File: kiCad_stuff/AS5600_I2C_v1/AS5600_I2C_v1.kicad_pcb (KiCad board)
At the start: 2 copper layers, 8 parts, among them J1 Conn_01x04, U1 AS5600_ASOM_v1

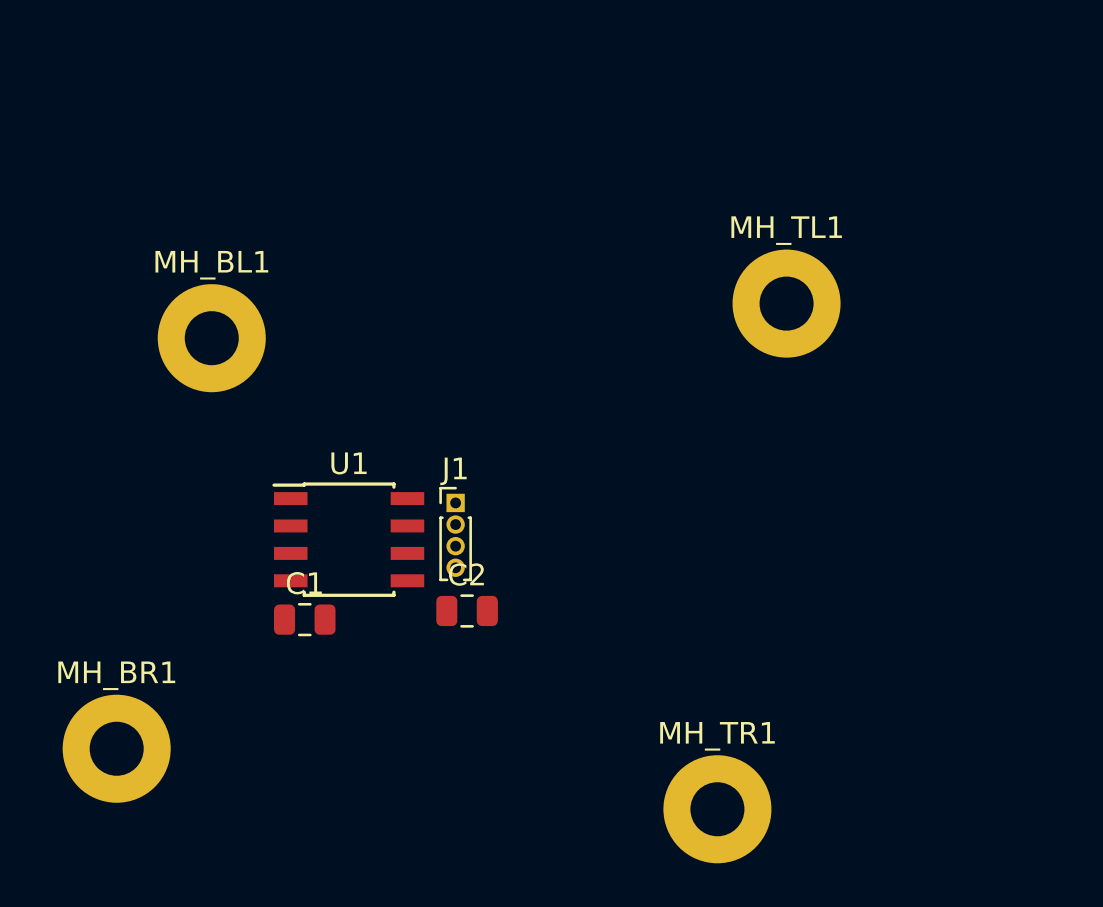
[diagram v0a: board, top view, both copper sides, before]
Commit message: Added proj footptint symbol lib with 2 user-made footprints
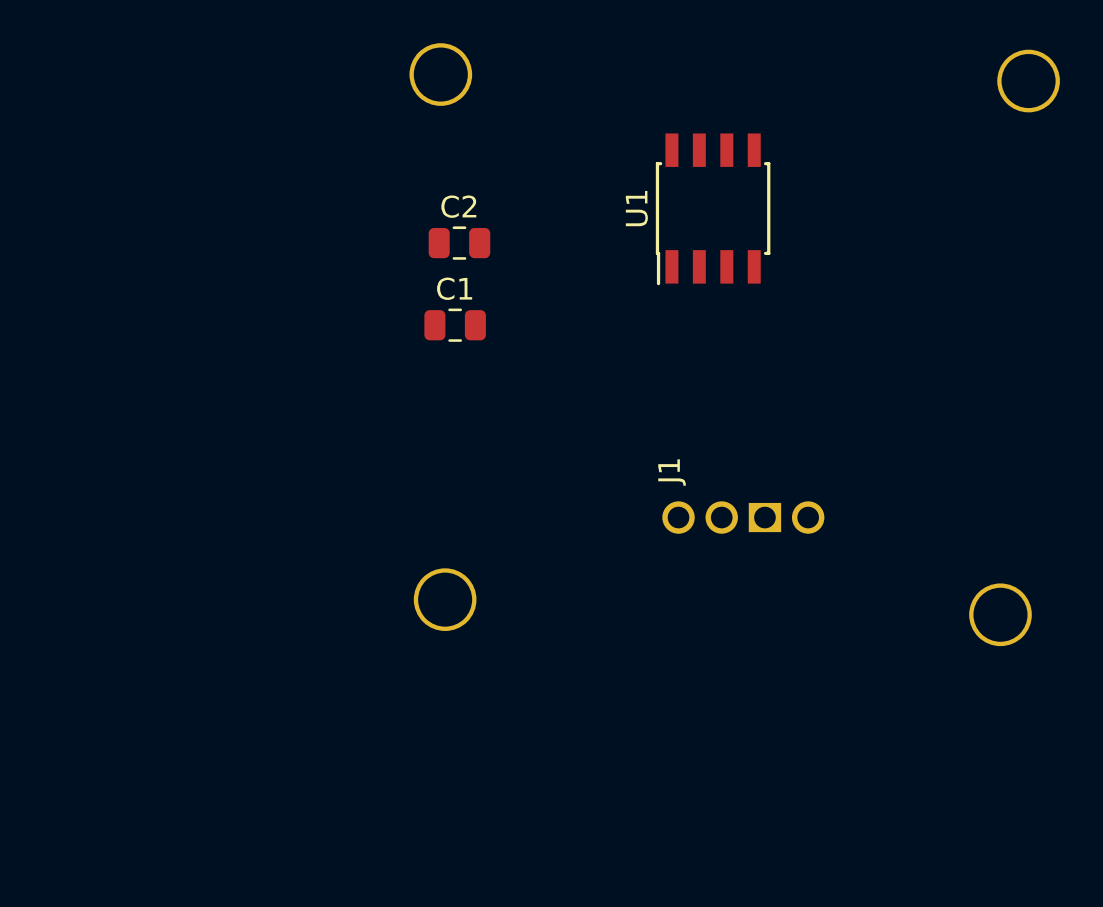
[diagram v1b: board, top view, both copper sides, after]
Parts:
- removed MH_BL1, MH_BR1, MH_TL1, MH_TR1: MountingHole, MountingHole:MountingHole_2.5mm_Pad
- added 2.5mm : Hole_TR, modular_segment_PCB_footprints:MountingHole_2.5mm_Pad, F.Cu at (184.2, 63.1)
- added 2.5mm : Hole_TL, modular_segment_PCB_footprints:MountingHole_2.5mm_Pad, F.Cu at (157.0, 62.8)
- added 2.5mm : Hole_BL, modular_segment_PCB_footprints:MountingHole_2.5mm_Pad, F.Cu at (157.2, 87.1)
- added 2.5mm : Hole_BR, modular_segment_PCB_footprints:MountingHole_2.5mm_Pad, F.Cu at (182.9, 87.8)
- J1: footprint Connector_PinHeader_1.00mm:PinHeader_1x04_P1.00mm_Vertical -> modular_segment_PCB_footprints:EthernetWireConnectors_1x04_P2.00mm_1mmDiam
- moved U1 22.8 mm to (169.6, 69.0), turned to 90 degrees
- moved C2 17.0 mm to (157.9, 70.6)
- moved C1 15.3 mm to (157.7, 74.4)
- moved J1 12.3 mm to (170.0, 83.3), turned to 90 degrees
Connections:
- U1 pad 5: (no net) -> Net-(U1-Pad5)

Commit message: Parts except pins in position
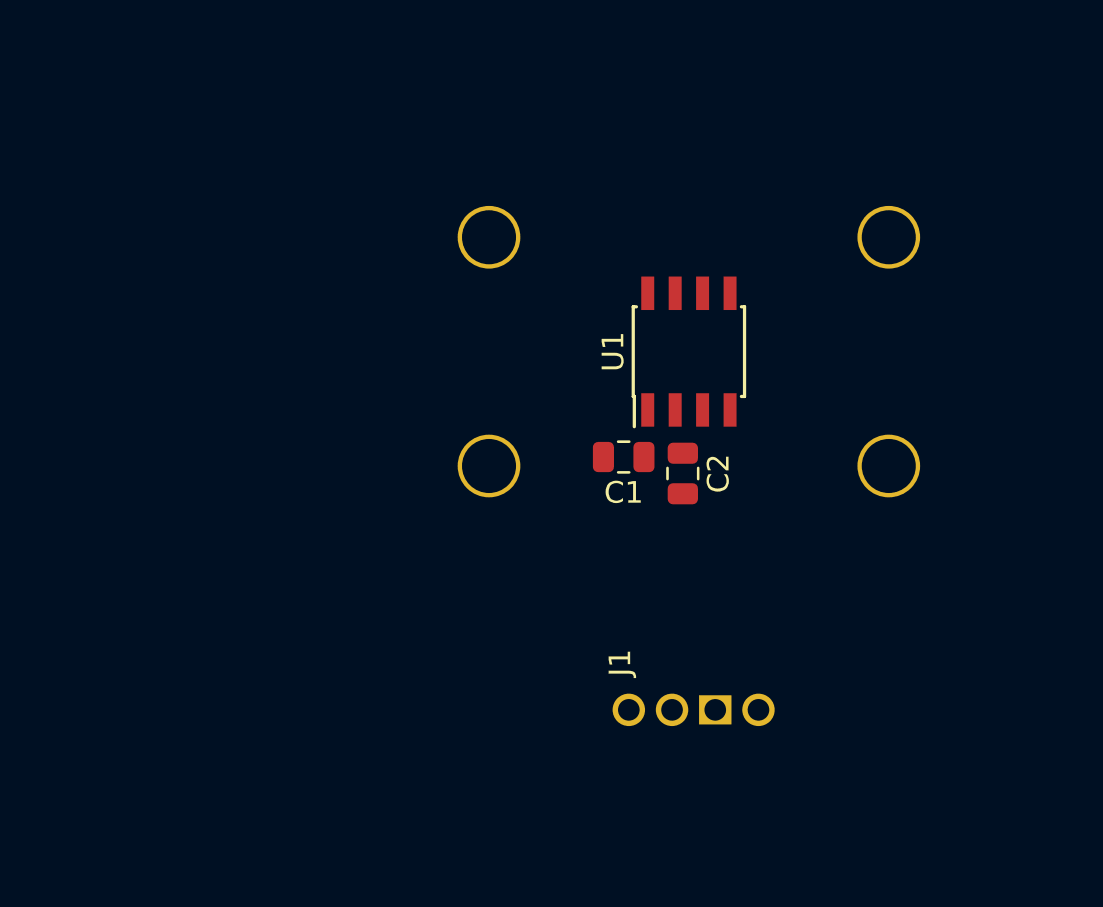
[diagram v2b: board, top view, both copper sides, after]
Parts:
- removed the 2.5mm  at (157.0, 62.8)
- removed the 2.5mm  at (157.2, 87.1)
- added 2.5mm : Hole_TL, modular_segment_PCB_footprints:MountingHole_2.5mm_Pad, F.Cu at (159.2, 70.3)
- added 2.5mm : Hole_BL, modular_segment_PCB_footprints:MountingHole_2.5mm_Pad, F.Cu at (159.2, 80.9)
- moved C2 14.9 mm to (168.2, 81.3), turned to 270 degrees
- moved C1 9.90 mm to (165.5, 80.5), turned to 180 degrees
- moved 2.5mm  9.70 mm to (177.7, 70.3)
- moved J1 9.19 mm to (167.7, 92.2)
- moved 2.5mm  8.61 mm to (177.7, 80.9)
- moved U1 6.72 mm to (168.5, 75.6)
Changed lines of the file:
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@@
     (pad_to_mask_clearance 0.2)
     (aux_axis_origin 0 0)
+    (grid_origin 152 59)
     (visible_elements 7FFFFFFF)
     (pcbplotparams
@@
     (add_net SDA)
   )
-  (module Capacitor_SMD:C_0805_2012Metric (layer F.Cu)
-    (at 157.6625 74.4)
+  (module Capacitor_SMD:C_0805_2012Metric locked (layer F.Cu)
+    (at 165.4625 80.5 180)
     (descr "Capacitor SMD 0805 (2012 Metric), square (rectangular) end terminal, IPC_7351 nominal, (Body size source: https://docs.google.com/spreadsheets/d/1BsfQQcO9C6DZCsRaXUlFlo91Tg2WpOkGARC1WS5S8t0/edit?usp=sharing), generated with kicad-footprint-generator")
     (tags capacitor)
     (attr smd)
-    (fp_text reference C1 (at 0 -1.65) (layer F.SilkS)
-      (effects (font (size 1 1) (thickness 0.15)))
-    )
-    (fp_text value 100nF (at 0 1.65) (layer F.Fab)
+    (fp_text reference C1 (at 0 -1.65 180) (layer F.SilkS)
+      (effects (font (size 1 1) (thickness 0.15)))
+    )
+    (fp_text value 100nF (at 0 1.65 180) (layer F.Fab)
       (effects (font (size 1 1) (thickness 0.15)))
     )
@@
     (fp_line (start 1.68 -0.95) (end 1.68 0.95) (layer F.CrtYd) (width 0.05))
     (fp_line (start 1.68 0.95) (end -1.68 0.95) (layer F.CrtYd) (width 0.05))
-    (fp_text user %R (at 0 0) (layer F.Fab)
+    (fp_text user %R (at 0 0 180) (layer F.Fab)
       (effects (font (size 0.5 0.5) (thickness 0.08)))
     )
-    (pad 1 smd roundrect (at -0.9375 0) (size 0.975 1.4) (layers F.Cu F.Paste F.Mask) (roundrect_rratio 0.25)
+    (pad 1 smd roundrect (at -0.9375 0 180) (size 0.975 1.4) (layers F.Cu F.Paste F.Mask) (roundrect_rratio 0.25)
       (net 1 +5V))
-    (pad 2 smd roundrect (at 0.9375 0) (size 0.975 1.4) (layers F.Cu F.Paste F.Mask) (roundrect_rratio 0.25)
+    (pad 2 smd roundrect (at 0.9375 0 180) (size 0.975 1.4) (layers F.Cu F.Paste F.Mask) (roundrect_rratio 0.25)
       (net 2 GND))
     (model ${KISYS3DMOD}/Capacitor_SMD.3dshapes/C_0805_2012Metric.wrl
@@
     )
   )
-  (module Capacitor_SMD:C_0805_2012Metric (layer F.Cu)
-    (at 157.8625 70.6)
+  (module Capacitor_SMD:C_0805_2012Metric locked (layer F.Cu)
+    (at 168.2 81.2625 270)
     (descr "Capacitor SMD 0805 (2012 Metric), square (rectangular) end terminal, IPC_7351 nominal, (Body size source: https://docs.google.com/spreadsheets/d/1BsfQQcO9C6DZCsRaXUlFlo91Tg2WpOkGARC1WS5S8t0/edit?usp=sharing), generated with kicad-footprint-generator")
     (tags capacitor)
     (attr smd)
-    (fp_text reference C2 (at 0 -1.65) (layer F.SilkS)
-      (effects (font (size 1 1) (thickness 0.15)))
-    )
-    (fp_text value 1uF (at 0 1.65) (layer F.Fab)
-      (effects (font (size 1 1) (thickness 0.15)))
-    )
-    (fp_text user %R (at 0 0) (layer F.Fab)
+    (fp_text reference C2 (at 0 -1.65 270) (layer F.SilkS)
+      (effects (font (size 1 1) (thickness 0.15)))
+    )
+    (fp_text value 1uF (at 0 1.65 270) (layer F.Fab)
+      (effects (font (size 1 1) (thickness 0.15)))
+    )
+    (fp_text user %R (at 0 0 270) (layer F.Fab)
       (effects (font (size 0.5 0.5) (thickness 0.08)))
     )
@@
     (fp_line (start -1 -0.6) (end 1 -0.6) (layer F.Fab) (width 0.1))
     (fp_line (start -1 0.6) (end -1 -0.6) (layer F.Fab) (width 0.1))
-    (pad 2 smd roundrect (at 0.9375 0) (size 0.975 1.4) (layers F.Cu F.Paste F.Mask) (roundrect_rratio 0.25)
-      (net 2 GND))
-    (pad 1 smd roundrect (at -0.9375 0) (size 0.975 1.4) (layers F.Cu F.Paste F.Mask) (roundrect_rratio 0.25)
+    (pad 2 smd roundrect (at 0.9375 0 270) (size 0.975 1.4) (layers F.Cu F.Paste F.Mask) (roundrect_rratio 0.25)
+      (net 2 GND))
+    (pad 1 smd roundrect (at -0.9375 0 270) (size 0.975 1.4) (layers F.Cu F.Paste F.Mask) (roundrect_rratio 0.25)
       (net 3 "Net-(C2-Pad1)"))
     (model ${KISYS3DMOD}/Capacitor_SMD.3dshapes/C_0805_2012Metric.wrl
@@
   )
   (module modular_segment_PCB_footprints:EthernetWireConnectors_1x04_P2.00mm_1mmDiam (layer F.Cu)
-    (at 170 83.3 90)
+    (at 167.7 92.2 90)
     (descr "Through hole straight pin header, 1x04, 1.00mm pitch, single row")
     (tags "Through hole pin header THT 1x04 1.00mm single row")
@@
     )
   )
-  (module Package_SO:SOIC-8_3.9x4.9mm_P1.27mm (layer F.Cu)
-    (at 169.6 69 90)
+  (module Package_SO:SOIC-8_3.9x4.9mm_P1.27mm locked (layer F.Cu)
+    (at 168.48 75.622 90)
     (descr "8-Lead Plastic Small Outline (SN) - Narrow, 3.90 mm Body [SOIC] (see Microchip Packaging Specification 00000049BS.pdf)")
     (tags "SOIC 1.27")
@@
     )
   )
-  (module modular_segment_PCB_footprints:MountingHole_2.5mm_Pad (layer F.Cu)
-    (at 184.2 63.1)
+  (module modular_segment_PCB_footprints:MountingHole_2.5mm_Pad locked (layer F.Cu)
+    (at 177.73 70.33)
     (descr "Mounting Hole 2.5mm")
     (tags "mounting hole 2.5mm")
@@
     (pad "" np_thru_hole circle (at 0 0) (size 2.9 2.9) (drill 2.5) (layers *.Cu *.Mask))
   )
-  (module modular_segment_PCB_footprints:MountingHole_2.5mm_Pad (layer F.Cu)
-    (at 157 62.8)
+  (module modular_segment_PCB_footprints:MountingHole_2.5mm_Pad locked (layer F.Cu)
+    (at 159.23 70.33)
     (descr "Mounting Hole 2.5mm")
     (tags "mounting hole 2.5mm")
@@
     (pad "" np_thru_hole circle (at 0 0) (size 2.9 2.9) (drill 2.5) (layers *.Cu *.Mask))
   )
-  (module modular_segment_PCB_footprints:MountingHole_2.5mm_Pad (layer F.Cu)
-    (at 157.2 87.1)
+  (module modular_segment_PCB_footprints:MountingHole_2.5mm_Pad locked (layer F.Cu)
+    (at 159.23 80.915)
     (descr "Mounting Hole 2.5mm")
     (tags "mounting hole 2.5mm")
@@
     (pad "" np_thru_hole circle (at 0 0) (size 2.9 2.9) (drill 2.5) (layers *.Cu *.Mask))
   )
-  (module modular_segment_PCB_footprints:MountingHole_2.5mm_Pad (layer F.Cu)
-    (at 182.9 87.8)
-    (descr "Mounting Hole 2.5mm")
-    (tags "mounting hole 2.5mm")
+  (module modular_segment_PCB_footprints:MountingHole_2.5mm_Pad locked (layer F.Cu)
+    (at 177.73 80.915)
+    (descr "Mounting Hole 2.5mm")
+    (tags "mounting hole 2.5mm")

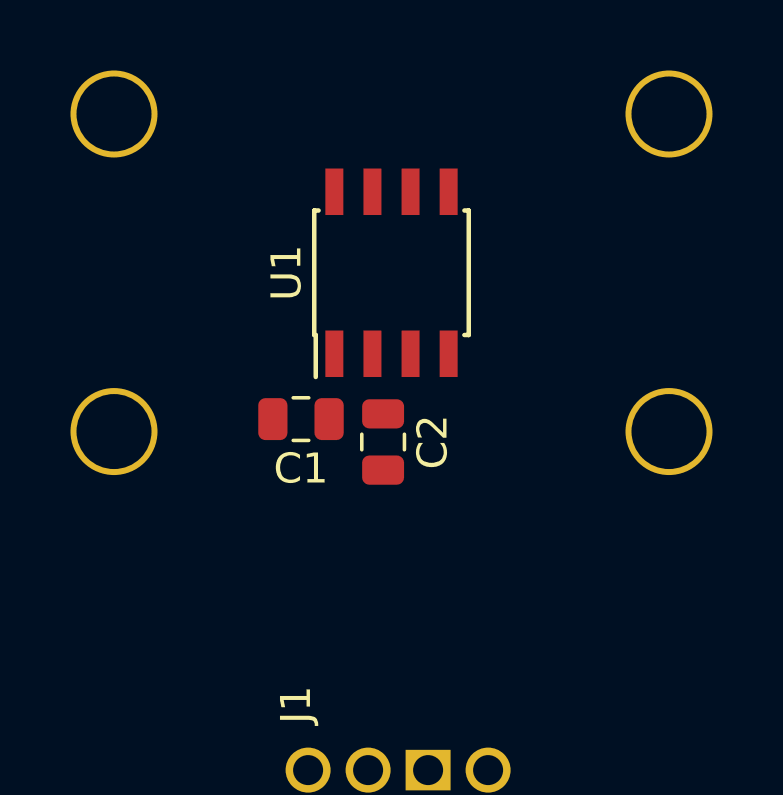
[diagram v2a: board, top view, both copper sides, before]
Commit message: Added PCB perimeter
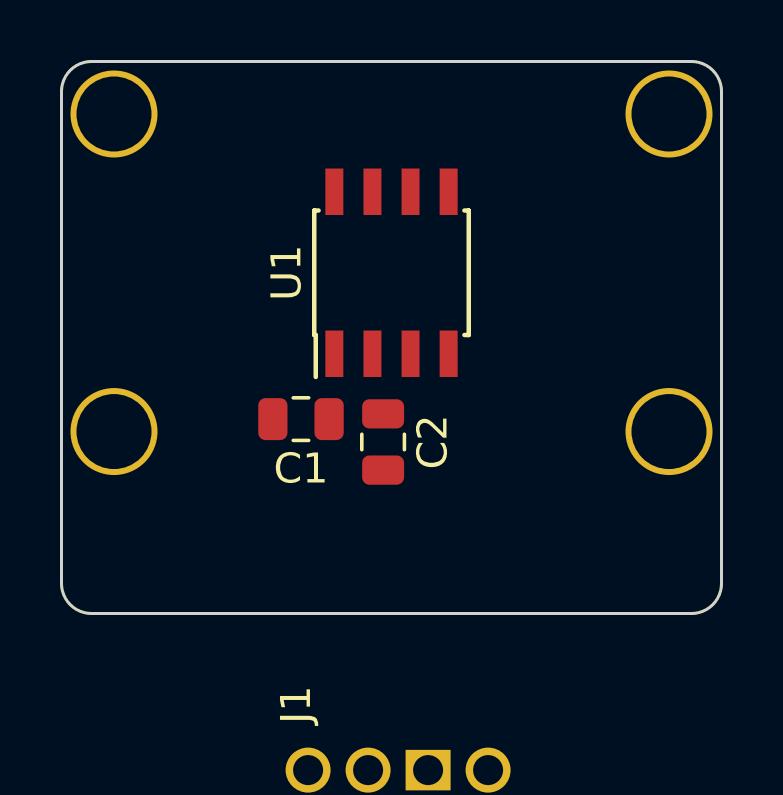
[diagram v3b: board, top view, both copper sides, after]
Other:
- board outline added: 22 x 18.4 mm
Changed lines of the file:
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@@
   (general
     (thickness 1.6)
-    (drawings 0)
+    (drawings 8)
     (tracks 0)
     (zones 0)
@@
     (trace_min 0.2)
     (segment_width 0.2)
-    (edge_width 0.15)
+    (edge_width 0.1)
     (via_size 0.8)
     (via_drill 0.4)
@@
     (pad "" np_thru_hole circle (at 0 0) (size 2.9 2.9) (drill 2.5) (layers *.Cu *.Mask))
   )
+  (gr_arc (start 178.48 69.58) (end 179.48 69.58) (angle -90) (layer Edge.Cuts) (width 0.1))
+  (gr_arc (start 158.48 69.58) (end 158.48 68.58) (angle -90) (layer Edge.Cuts) (width 0.1))
+  (gr_arc (start 158.48 85.98) (end 157.48 85.98) (angle -90) (layer Edge.Cuts) (width 0.1))
+  (gr_arc (start 178.48 85.98) (end 178.48 86.98) (angle -90) (layer Edge.Cuts) (width 0.1))
+  (gr_line (start 157.48 69.58) (end 157.48 85.98) (layer Edge.Cuts) (width 0.1))
+  (gr_line (start 158.48 86.98) (end 178.48 86.98) (layer Edge.Cuts) (width 0.1))
+  (gr_line (start 179.48 85.98) (end 179.48 69.58) (layer Edge.Cuts) (width 0.1))
+  (gr_line (start 178.48 68.58) (end 158.48 68.58) (layer Edge.Cuts) (width 0.1))
 )

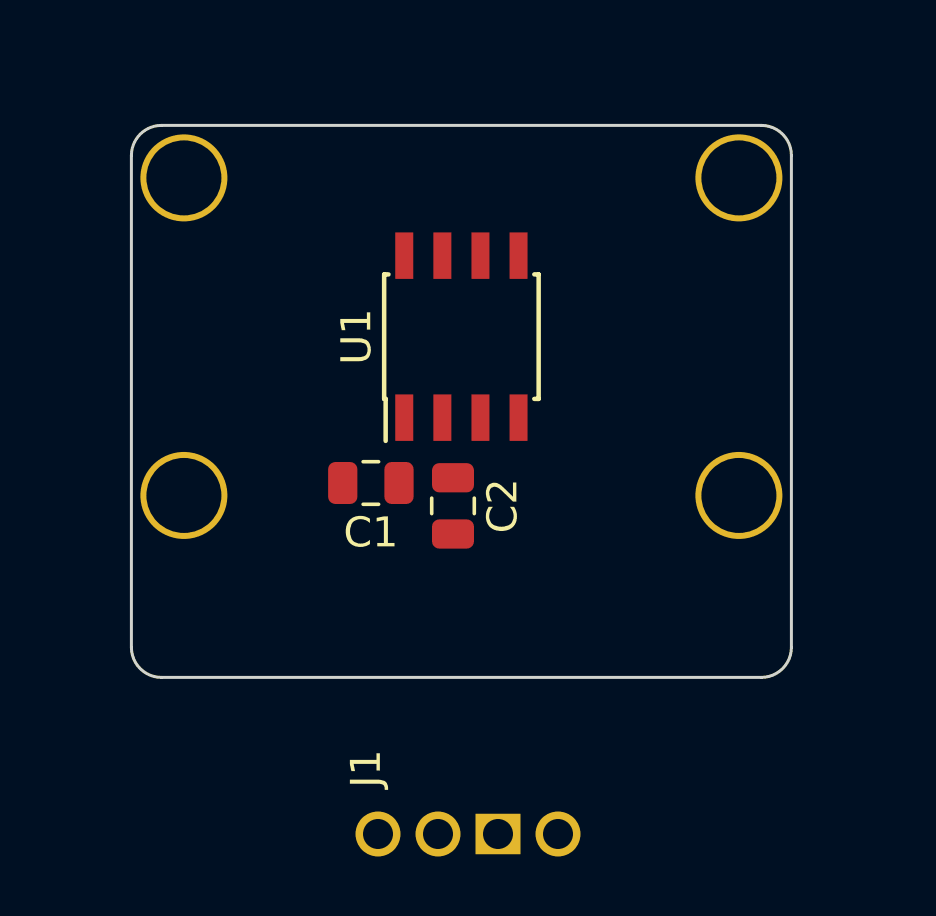
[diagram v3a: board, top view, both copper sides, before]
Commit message: Ethernet-cable direct solder v2 completed
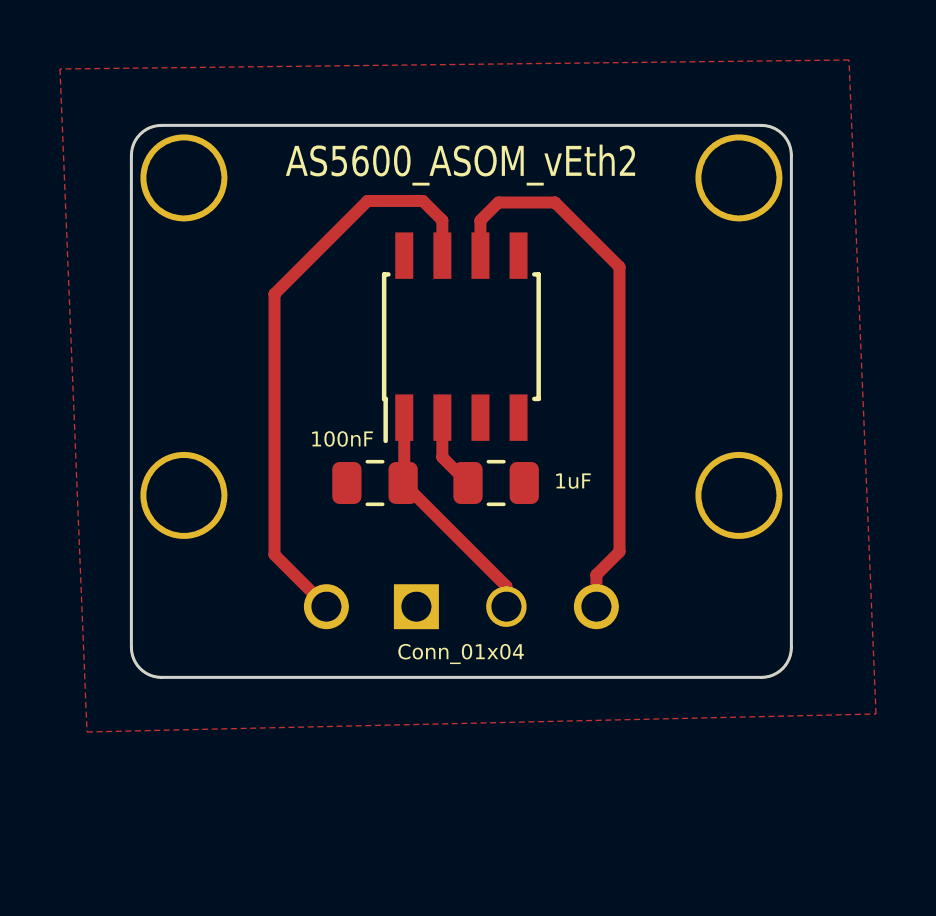
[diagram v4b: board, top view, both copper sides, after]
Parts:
- U1: value AS5600_ASOM_v1 -> AS5600_ASOM_vEth2
- moved J1 7.62 mm to (168.5, 84.6), turned to 0 degrees
- moved C2 1.63 mm to (169.6, 80.5), turned to 0 degrees
- moved C1 0.14 mm to (165.6, 80.5)
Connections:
- J1 pad 1: SDA -> SCL
- J1 pad 2: +5V -> GND
- J1 pad 3: GND -> +5V
- J1 pad 4: SCL -> SDA
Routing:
- net SCL: track 0.00 -> 19.5 mm
- net SDA: track 0.00 -> 18.6 mm
- net +5V: track 0.00 -> 7.80 mm
- net Net-(C2-Pad1): track 0.00 -> 2.53 mm
- added copper zone on F.Cu, net GND
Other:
- net class Default: clearance 0.2 -> 0.3; trace_width 0.25 -> 0.4
- rule trace_clearance: 0.2 -> 0.3
